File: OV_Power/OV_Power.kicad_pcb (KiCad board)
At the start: 2 copper layers, 174 x 57.5 mm, 85 parts, among them CN1 CONN_HEADER_R_A_2POS_2.5MM, J1 Kycon_kpjx-4s_shielded, J2 Conn_HDR_2x10_latching, J3 532530670, J4 SpadeLug, J5 SpadeLug, J6 CONN_HEADER_2.54X2_MOLEX_KK_S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, J7 CONN_HEADER_2.54X2_MOLEX_KK_S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, Q1 SSM3K341R, Q2 2N7002BK, Q3 SZNUD3124LT1G, Q4 SZNUD3124LT1G, U1 LT3796, U2 LT1936, U3 LT6106, U4 VNH5019ATR-E, U7 LTC4416, U8 AOSD21307, U9 AOSD21307

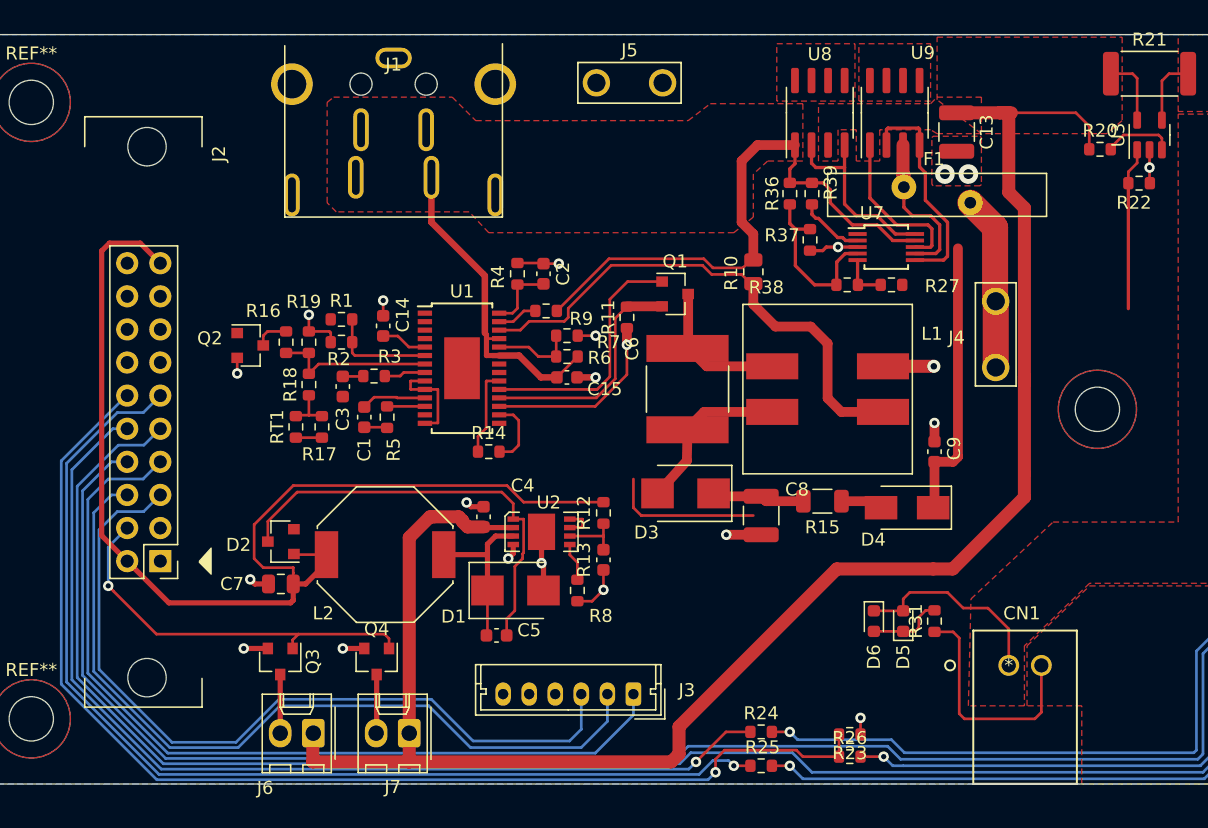
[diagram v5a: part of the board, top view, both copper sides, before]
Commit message: Power board routing is finished in 2 layers, but pcb outline is apparently changing yet again...
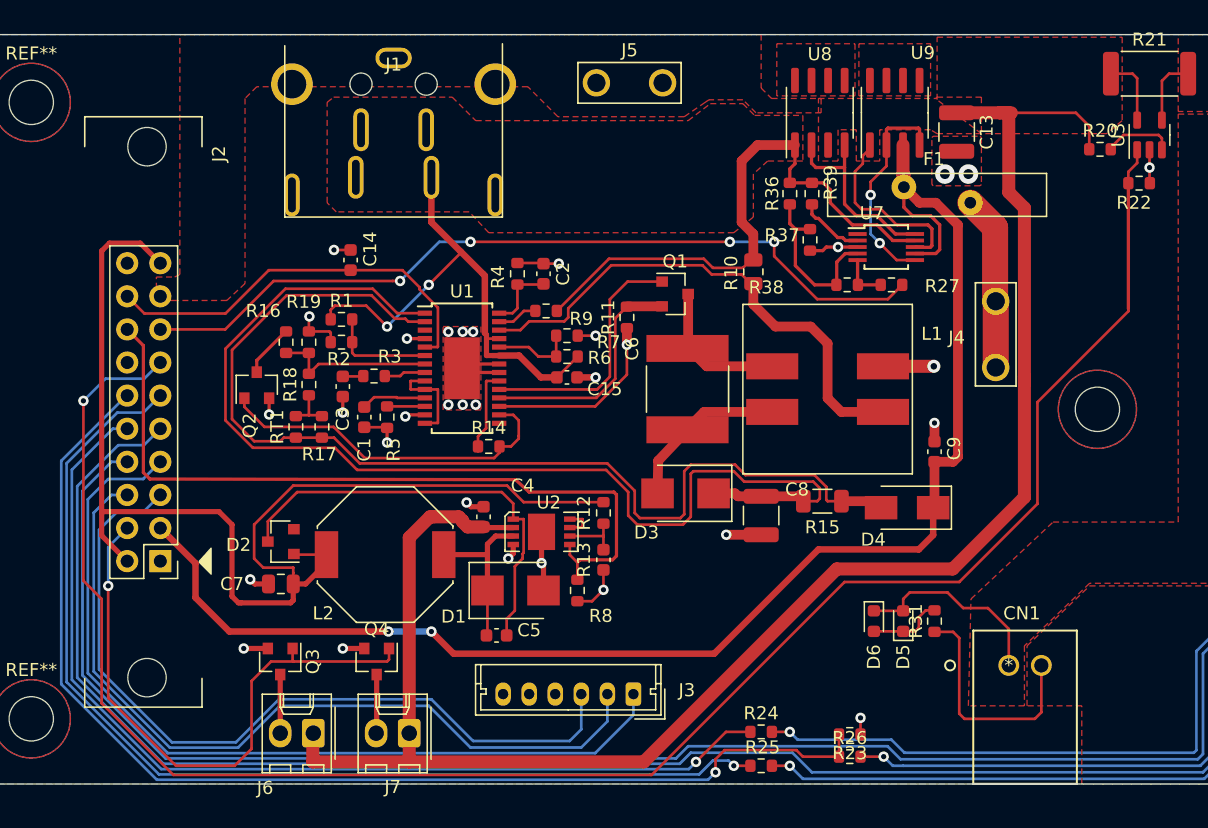
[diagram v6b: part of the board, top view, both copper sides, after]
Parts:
- moved C14 5.63 mm to (59.7, 47.3)
- moved Q2 3.09 mm to (52.5, 56.9), turned to 90 degrees
- moved R14 0.40 mm to (70.3, 61.6)
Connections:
- net Net-(C8-Pad1) renamed /ISP_P
- net Net-(D4-Pad2) renamed /ISP_N
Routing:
- net MOTOR_CURRENT: track 12.5 -> 143.9 mm, vias 0 -> 1
- net VBATT: track 34.6 -> 112.4 mm, vias 0 -> 2
- net /ISP_N: track 5.24 -> 82.4 mm
- net /ISP_P: track 19.4 -> 86.9 mm
- net /Power Supply/POWER_STATUS: track 0.00 -> 62.6 mm, vias 0 -> 4
- net V7.5V_EN: track 2.94 -> 59.3 mm
- net CHG_CURRENT: track 3.50 -> 31.1 mm
- net Net-(Q2-Pad1): track 5.26 -> 27.3 mm
- net /Power Supply/FAN_DRIVE: track 30.3 -> 45.6 mm
- net VIN_12V: track 69.7 -> 83.7 mm, vias 0 -> 2
- net GND: track 99.3 -> 109.9 mm, vias 35 -> 45
- net V7.5V: track 87.5 -> 94.3 mm
- net Net-(Q2-Pad3): track 2.63 -> 4.07 mm
- net V_MAIN: track 154.5 -> 155.1 mm
- net Net-(U7-Pad6): track 17.1 -> 16.6 mm, vias 0 -> 2
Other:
- net class Default: clearance 0.2 -> 0.208; trace_width 0.25 -> 0.208
- rule solder_mask_min_width: 0.25 -> 0.153
- rule trace_clearance: 0.2 -> 0.208

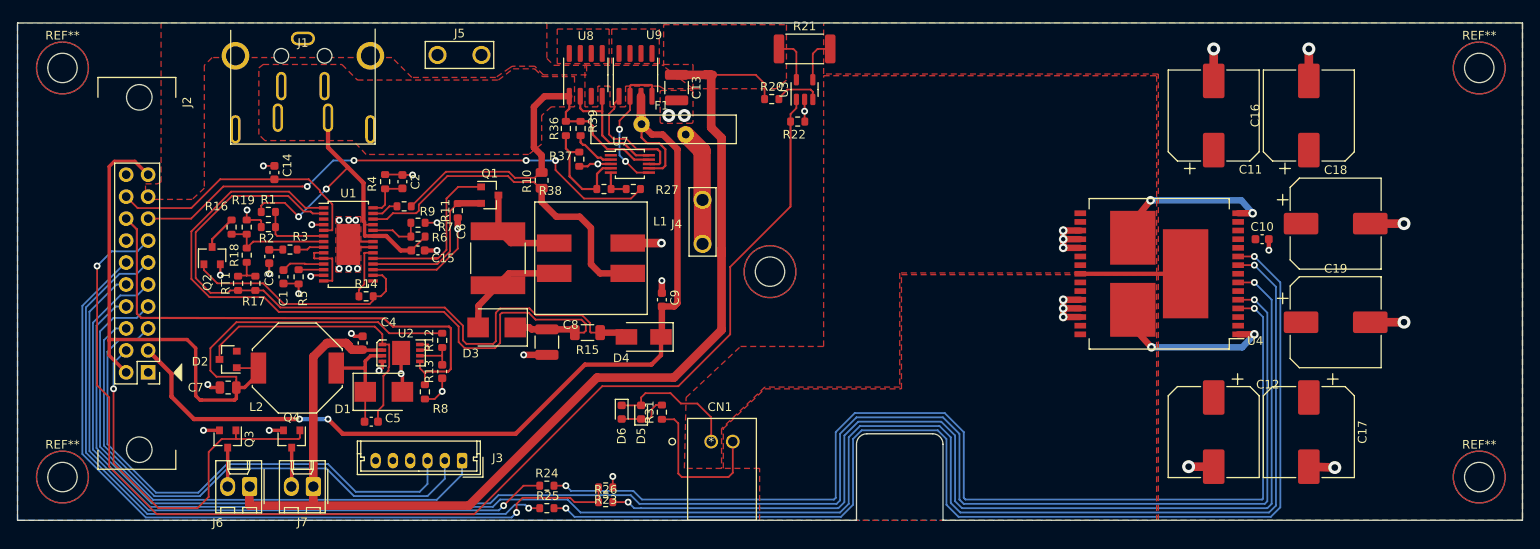
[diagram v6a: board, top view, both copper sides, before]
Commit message: The power board is finished, output generated.  Still need to make a sensible bill of materials but that is probably best done from the schematic at this stage.
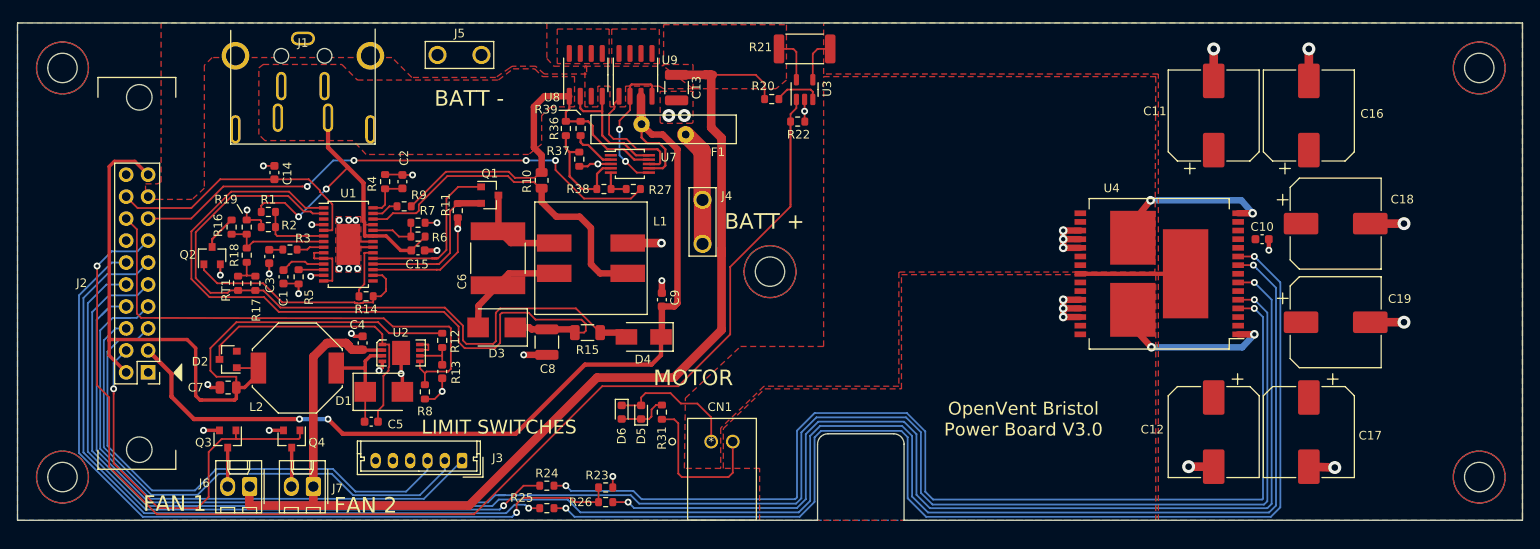
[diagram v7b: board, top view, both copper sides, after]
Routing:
- net nMOTOR-FAULT-A: track 200.5 -> 202.6 mm
- net Net-(J2-Pad5): track 61.6 -> 60.1 mm
- net PWM: track 90.4 -> 91.8 mm
- net Net-(J2-Pad6): track 62.7 -> 61.5 mm
- net MOTOR-IN-B: track 82.1 -> 83.3 mm
- net Net-(J2-Pad7): track 67.3 -> 68.3 mm
- net MOTOR-IN-A: track 77.7 -> 78.7 mm
- net /ISP_N: track 82.4 -> 81.8 mm
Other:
- outline, holes or cut-outs redrawn
- rule pad_to_mask_clearance: 0.051 -> 0
- board text added: "BATT +"
- board text added: "BATT -"
- board text added: "FAN 1"
- board text added: "FAN 2"
- board text added: "LIMIT SWITCHES"
- board text added: "MOTOR"
- board text added: "OpenVent Bristol Power Board V3.0"

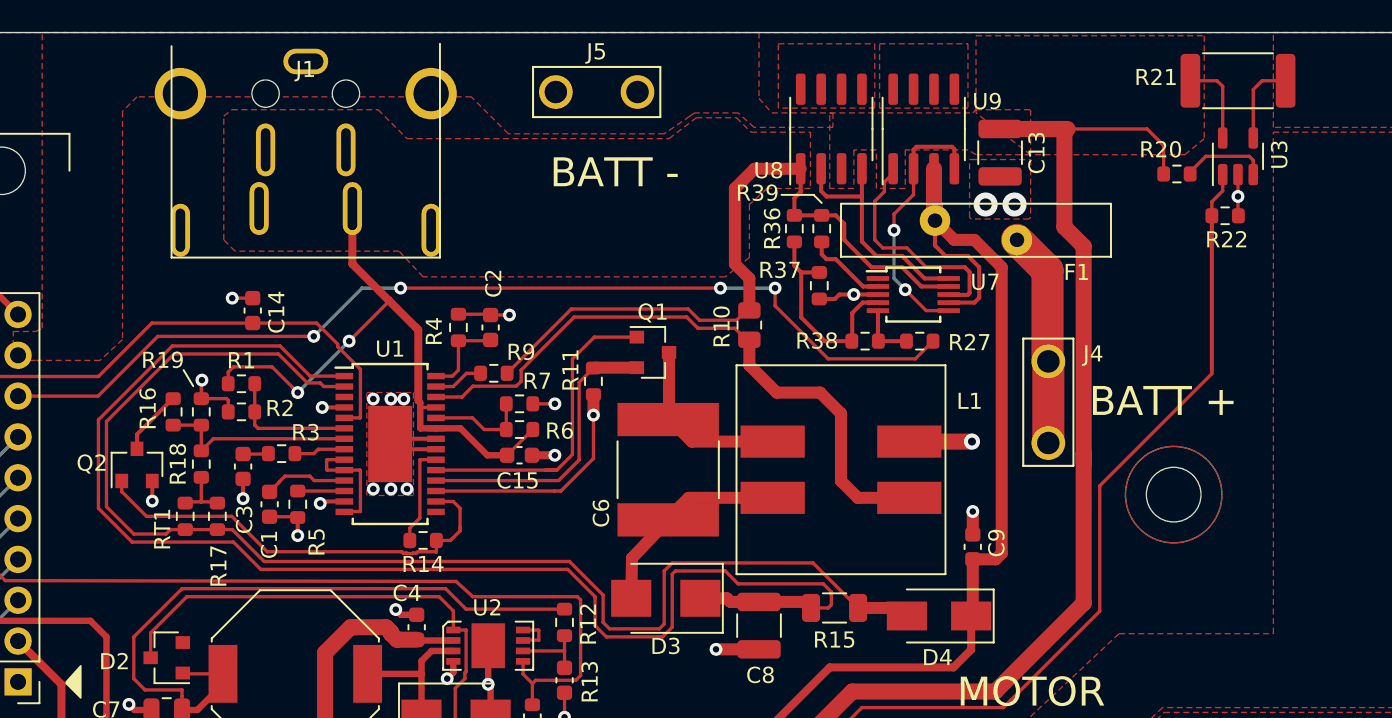
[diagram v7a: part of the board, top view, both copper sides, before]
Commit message: Slight change to schemo per Rick's suggestion, also generated the real BOM.  Gerbers updated, should be ready for production.
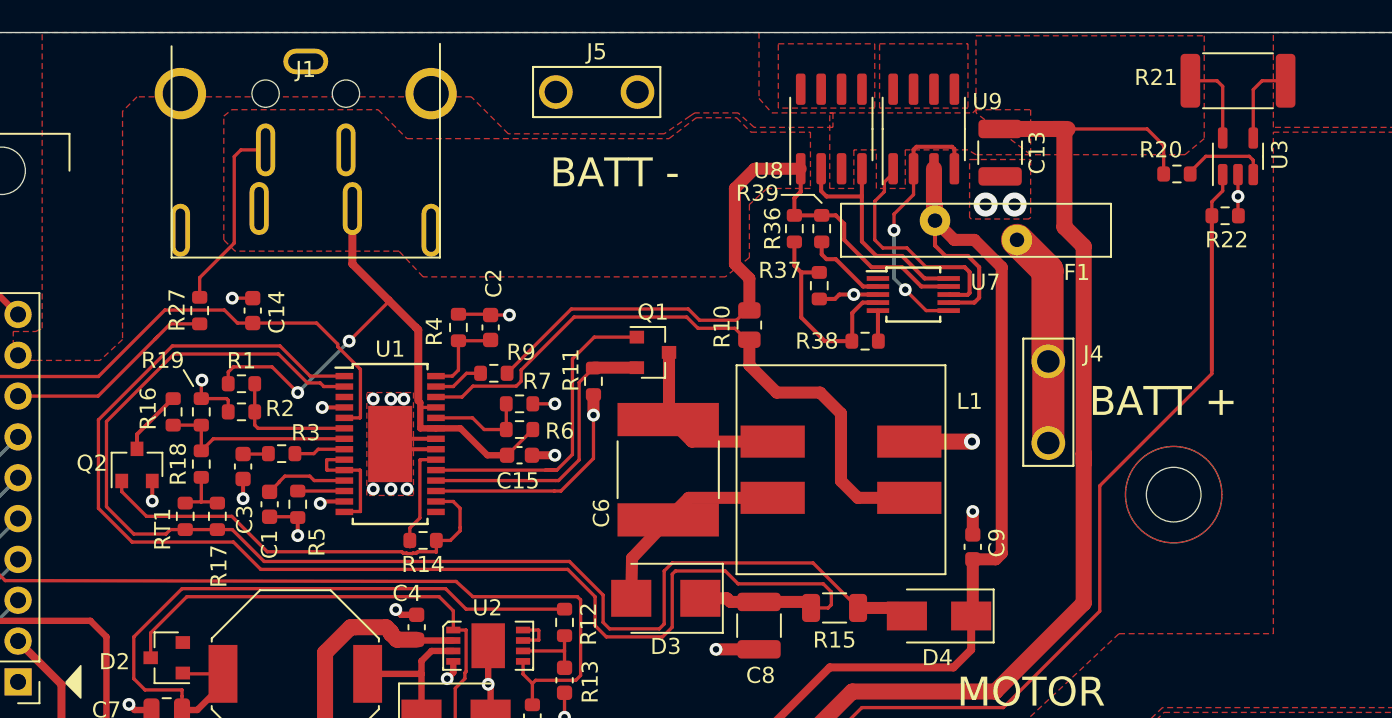
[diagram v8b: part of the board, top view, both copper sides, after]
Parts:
- moved R27 44.8 mm to (56.4, 47.3), turned to 90 degrees
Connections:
- R27 pad 2: Net-(R27-Pad2) -> VIN_12V
- R38 pad 1: Net-(R27-Pad2) -> Net-(R38-Pad1)
- U7 pad 5: Net-(R27-Pad2) -> Net-(R38-Pad1)
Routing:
- net /Power Supply/POWER_STATUS: track 62.6 -> 13.4 mm, vias 4 -> 0
- net VIN_12V: track 83.7 -> 95.4 mm
- net Net-(R27-Pad2): track 3.66 -> 0.00 mm
- net Net-(R38-Pad1): track 0.00 -> 1.91 mm
- net CHG_CURRENT: track 31.1 -> 31.7 mm
